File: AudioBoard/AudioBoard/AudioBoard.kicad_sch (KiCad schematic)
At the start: 0 parts

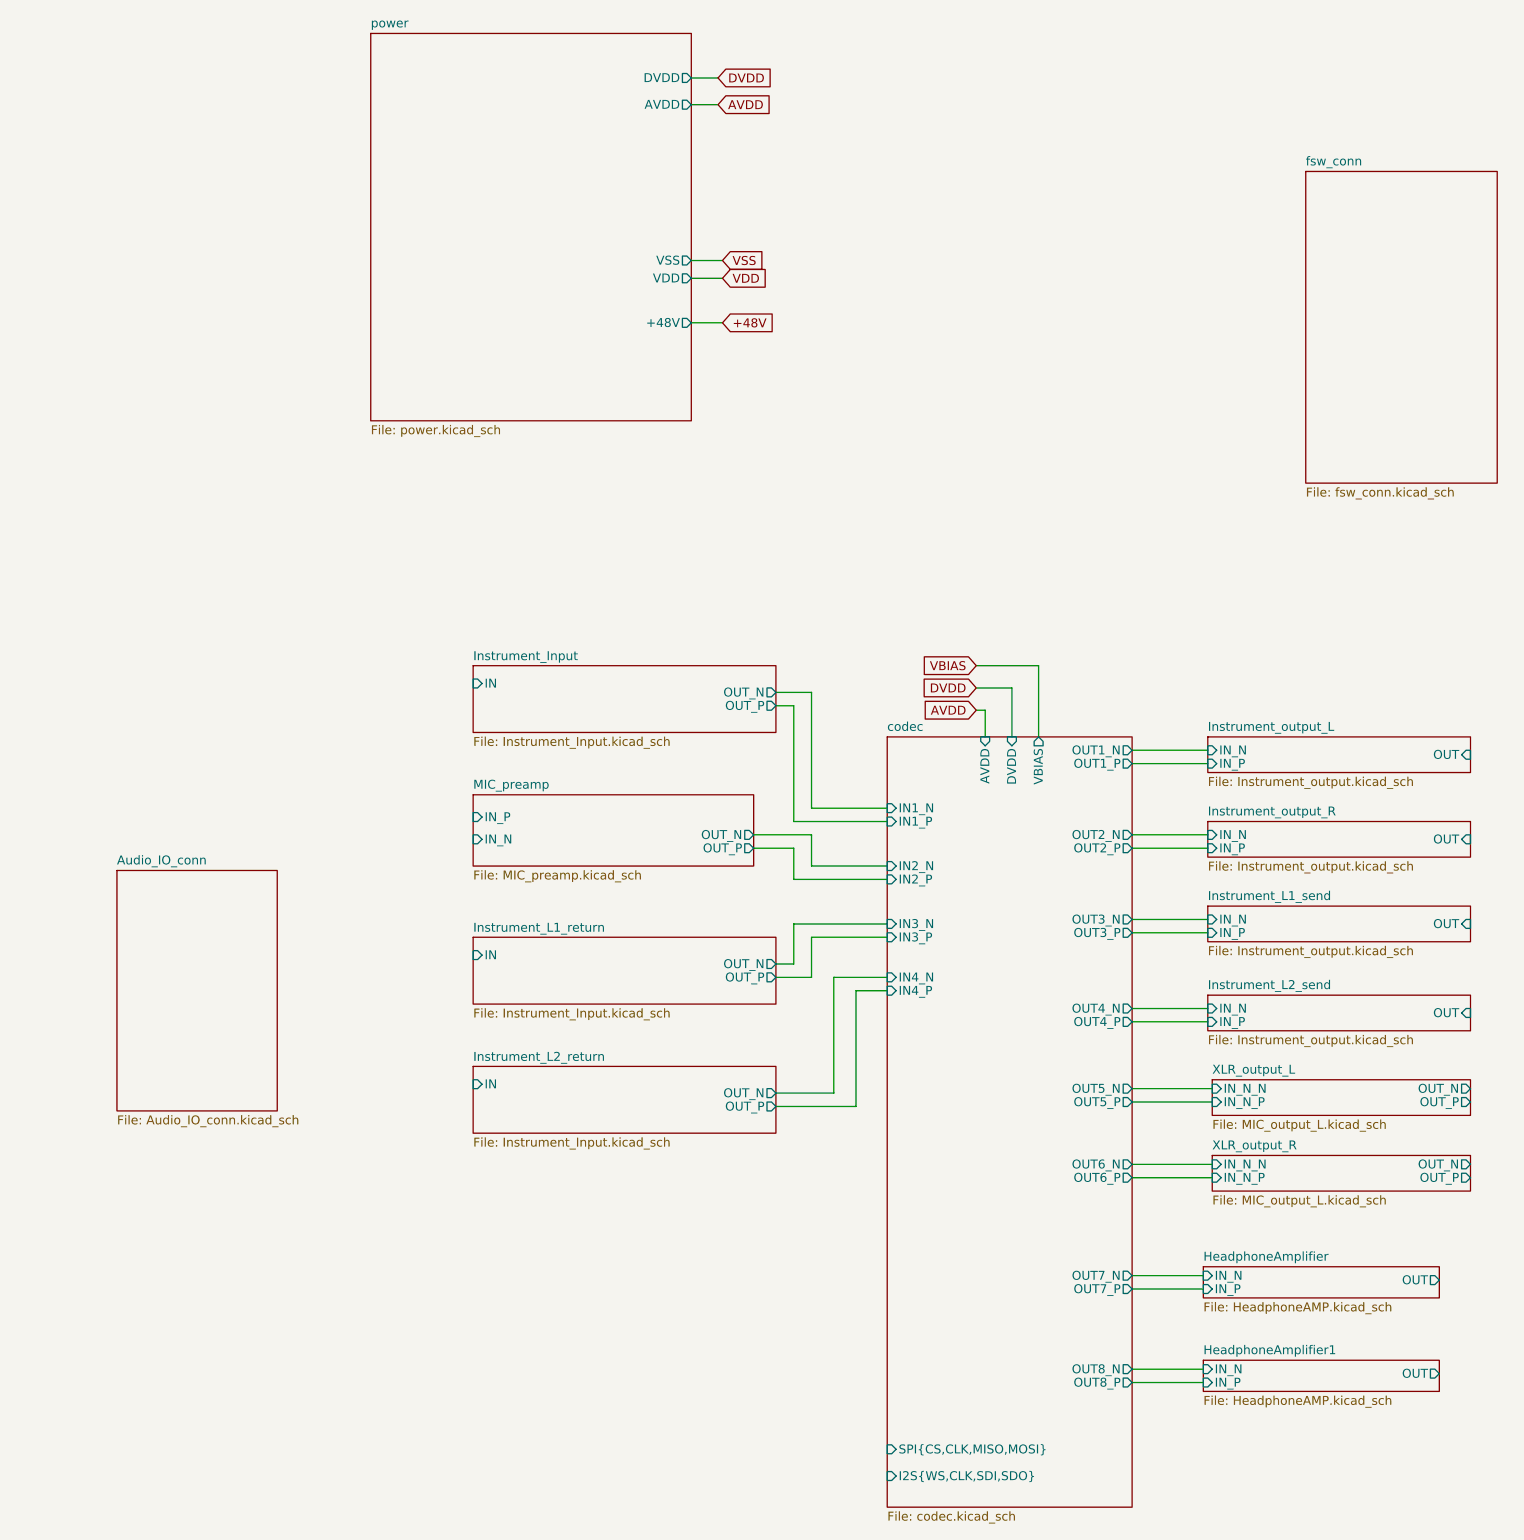
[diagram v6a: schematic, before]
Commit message: added jack IO, headphone amp cirucit
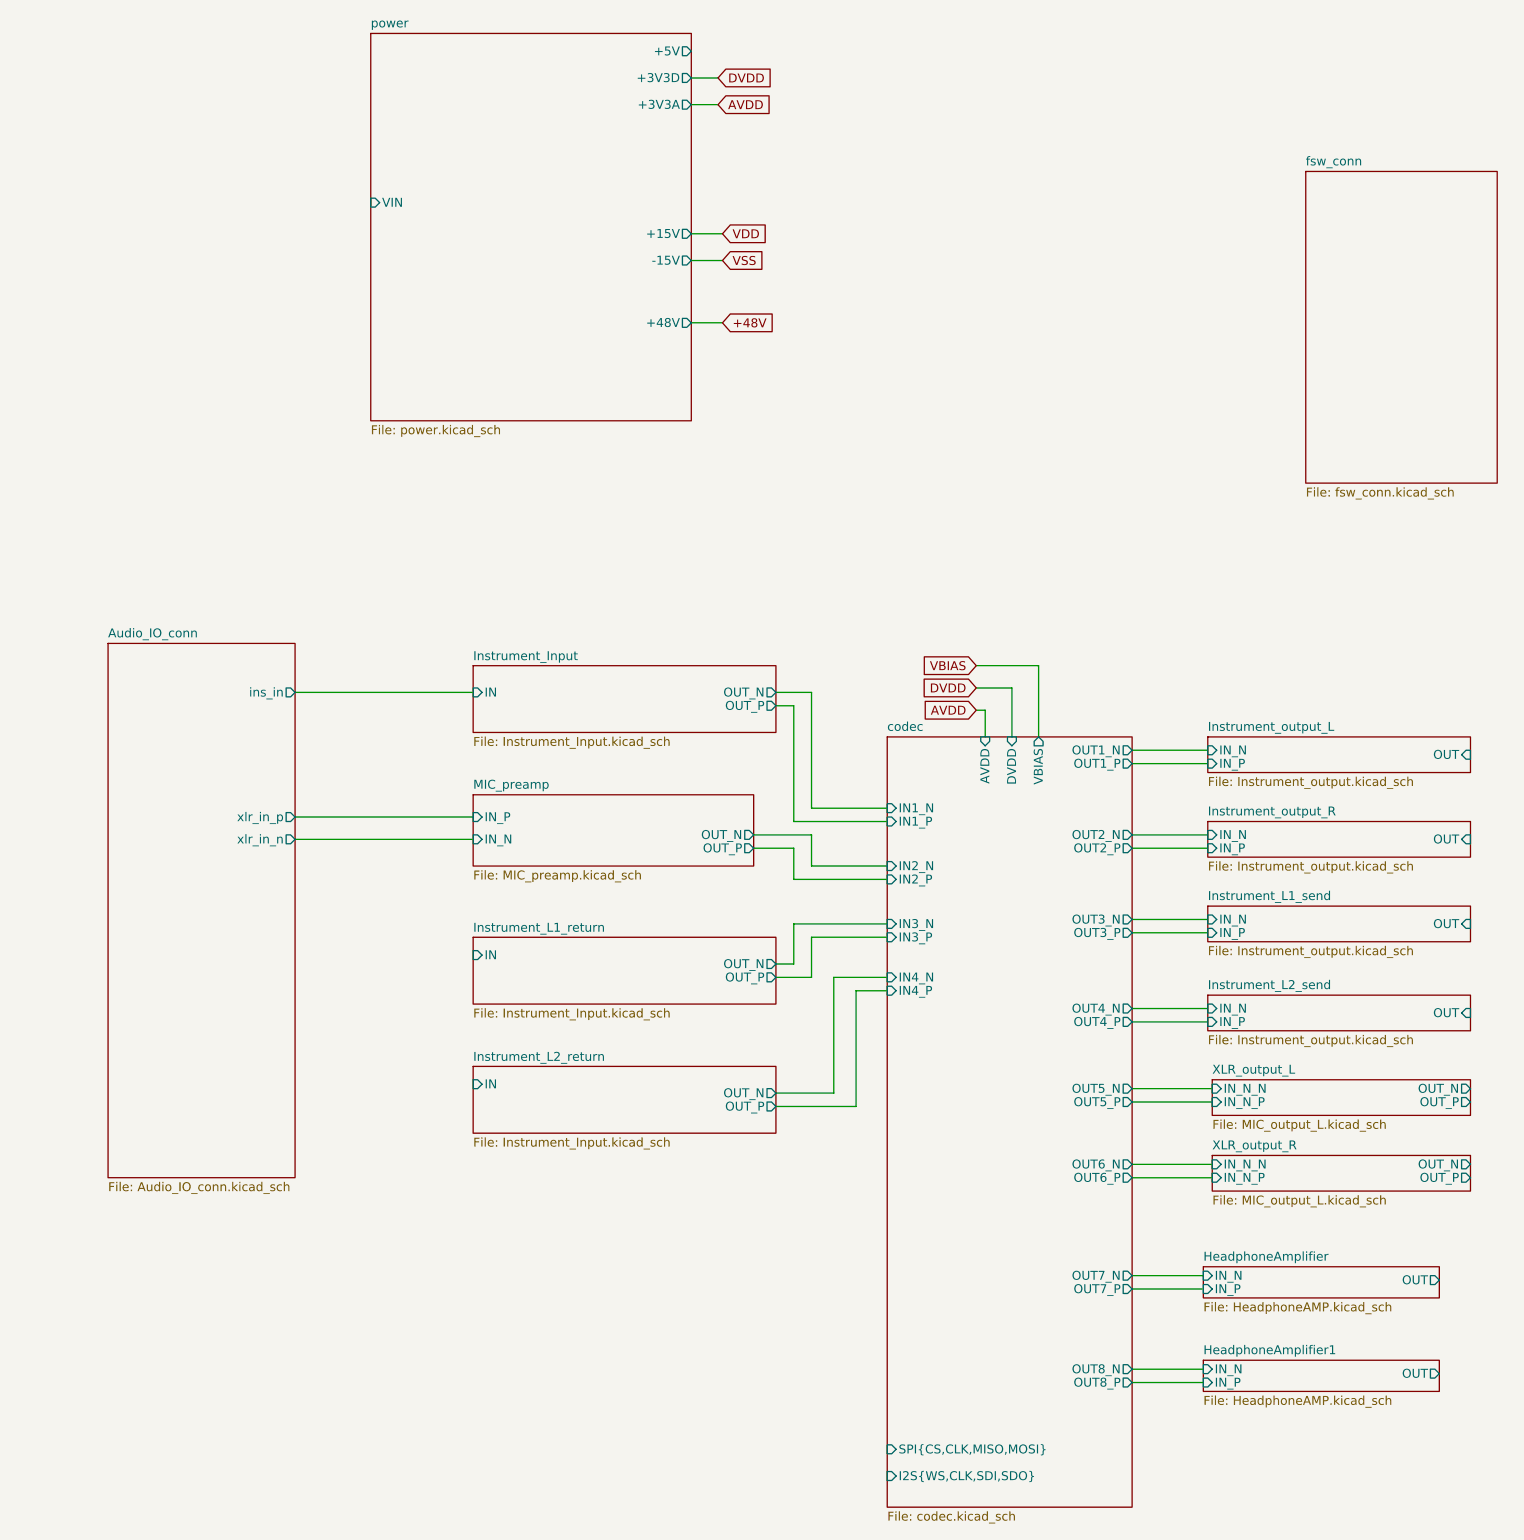
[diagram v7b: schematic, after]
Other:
- sheet Audio_IO_conn ports: added ins_in, xlr_in_n, xlr_in_p; removed none
- sheet power ports: added +15V, +3V3A, +3V3D, +5V, -15V, VIN; removed AVDD, DVDD, VDD, VSS
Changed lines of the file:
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@@
+	(wire
+		(pts
+			(xy 108.585 133.985) (xy 133.985 133.985)
+		)
+		(stroke
+			(width 0)
+			(type default)
+		)
+	)
 	(wire
 		(pts
@@
 	(wire
 		(pts
+			(xy 108.585 151.765) (xy 133.985 151.765)
+		)
+		(stroke
+			(width 0)
+			(type default)
+		)
+	)
+	(wire
+		(pts
 			(xy 179.705 172.72) (xy 177.165 172.72)
 		)
@@
 	(wire
 		(pts
-			(xy 169.545 74.93) (xy 165.1 74.93)
+			(xy 165.1 68.58) (xy 169.545 68.58)
+		)
+		(stroke
+			(width 0)
+			(type default)
+		)
+	)
+	(wire
+		(pts
+			(xy 108.585 154.94) (xy 133.985 154.94)
 		)
 		(stroke
@@
 	(global_label "VDD"
 		(shape input)
-		(at 169.545 74.93 0)
+		(at 169.545 68.58 0)
 		(fields_autoplaced yes)
 		(effects
@@
 		)
 		(property "Intersheetrefs" "${INTERSHEET_REFS}"
-			(at 176.1588 74.93 0)
+			(at 176.1588 68.58 0)
 			(hide yes)
 			(show_name no)
@@
 	)
 	(sheet
-		(at 83.185 159.385)
-		(size 22.86 34.29)
+		(at 81.915 127)
+		(size 26.67 76.2)
 		(exclude_from_sim no)
 		(in_bom yes)
@@
 		)
 		(property "Sheetname" "Audio_IO_conn"
-			(at 83.185 158.6734 0)
+			(at 81.915 126.2884 0)
 			(show_name no)
 			(do_not_autoplace no)
@@
 		)
 		(property "Sheetfile" "Audio_IO_conn.kicad_sch"
-			(at 83.185 194.2596 0)
+			(at 81.915 203.7846 0)
 			(show_name no)
 			(do_not_autoplace no)
@@
 				)
 				(justify left top)
+			)
+		)
+		(pin "ins_in" output
+			(at 108.585 133.985 0)
+			(effects
+				(font
+					(size 1.27 1.27)
+				)
+				(justify right)
+			)
+		)
+		(pin "xlr_in_n" output
+			(at 108.585 154.94 0)
+			(effects
+				(font
+					(size 1.27 1.27)
+				)
+				(justify right)
+			)
+		)
+		(pin "xlr_in_p" output
+			(at 108.585 151.765 0)
+			(effects
+				(font
+					(size 1.27 1.27)
+				)
+				(justify right)
 			)
 		)
@@
 		)
 		(pin "IN" input
-			(at 133.985 132.715 180)
+			(at 133.985 133.985 180)
 			(effects
 				(font
@@
 			)
 		)
-		(pin "AVDD" output
-			(at 165.1 50.165 0)
-			(effects
-				(font
-					(size 1.27 1.27)
-				)
-				(justify right)
-			)
-		)
-		(pin "DVDD" output
-			(at 165.1 46.355 0)
-			(effects
-				(font
-					(size 1.27 1.27)
-				)
-				(justify right)
-			)
-		)
-		(pin "VDD" output
-			(at 165.1 74.93 0)
-			(effects
-				(font
-					(size 1.27 1.27)
-				)
-				(justify right)
-			)
-		)
-		(pin "VSS" output
-			(at 165.1 72.39 0)
-			(effects
-				(font
-					(size 1.27 1.27)
-				)
-				(justify right)
-			)
-		)
 		(pin "+48V" output
 			(at 165.1 81.28 0)
@@
 			)
 		)
+		(pin "+3V3A" output
+			(at 165.1 50.165 0)
+			(effects
+				(font
+					(size 1.27 1.27)
+				)
+				(justify right)
+			)
+		)
+		(pin "+3V3D" output
+			(at 165.1 46.355 0)
+			(effects
+				(font
+					(size 1.27 1.27)
+				)
+				(justify right)
+			)
+		)
+		(pin "+5V" output
+			(at 165.1 42.545 0)
+			(effects
+				(font
+					(size 1.27 1.27)
+				)
+				(justify right)
+			)
+		)
+		(pin "+15V" output
+			(at 165.1 68.58 0)
+			(effects
+				(font
+					(size 1.27 1.27)
+				)
+				(justify right)
+			)
+		)
+		(pin "-15V" output
+			(at 165.1 72.39 0)
+			(effects
+				(font
+					(size 1.27 1.27)
+				)
+				(justify right)
+			)
+		)
+		(pin "VIN" input
+			(at 119.38 64.135 180)
+			(effects
+				(font
+					(size 1.27 1.27)
+				)
+				(justify left)
+			)
+		)

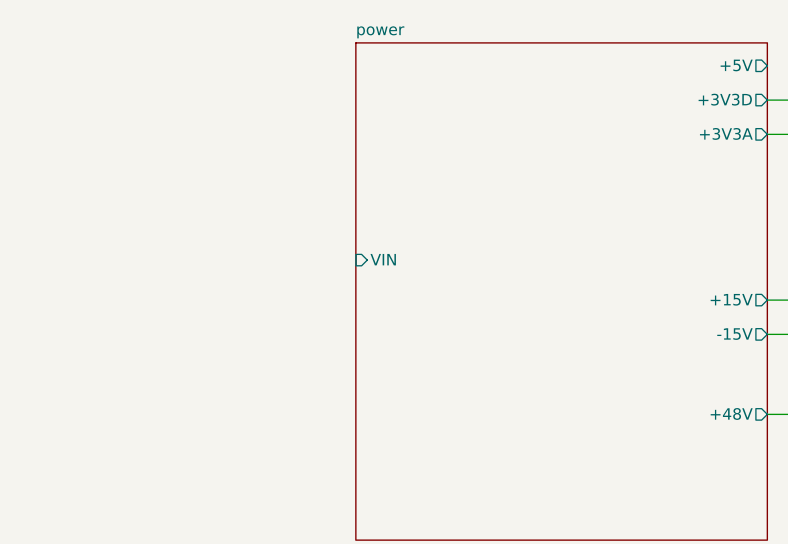
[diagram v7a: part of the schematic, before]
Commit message: added pwr sw and headphone out
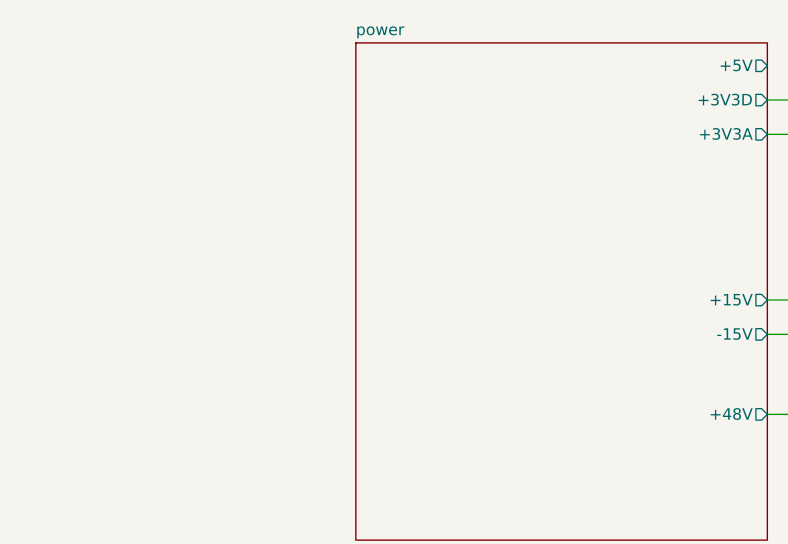
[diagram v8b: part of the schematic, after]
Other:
- sheet power ports: added none; removed VIN
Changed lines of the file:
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@@
-			)
-		)
-		(pin "VIN" input
-			(at 119.38 64.135 180)
-			(effects
-				(font
-					(size 1.27 1.27)
-				)
-				(justify left)
 			)
 		)
